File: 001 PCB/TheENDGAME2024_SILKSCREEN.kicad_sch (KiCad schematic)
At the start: 78 parts, among them J1 B+, J2 B-, SW1 SW_SPDT, SW10 SW_Push, SW11 SW_Push, SW12 SW_Push, SW13 SW_Push, SW14 SW_Push, SW15 SW_Push, SW16 SW_Push, SW17 SW_Push, SW18 SW_Push, SW19 SW_Push, SW2 SW_Push, SW20 SW_Push, SW21 SW_Push, SW22 SW_Push, SW23 SW_Push, SW24 SW_Push, SW25 SW_Push, SW26 SW_Push, SW27 SW_Push, SW28 SW_Push, SW29 SW_Push, SW3 SW_Push, SW30 SW_Push, SW31 SW_Push, SW32 SW_Push, SW33 SW_Push, SW34 SW_Push, SW35 SW_Push, SW36 SW_Push, SW37 SW_Push, SW38 SW_Push, SW4 SW_Push, SW5 SW_Push, SW6 SW_Push, SW7 SW_Push, SW8 SW_Push, SW9 SW_Push, U1 SuperMini nRF52840, U2 RP2040-Zero_stolen_from_Purox

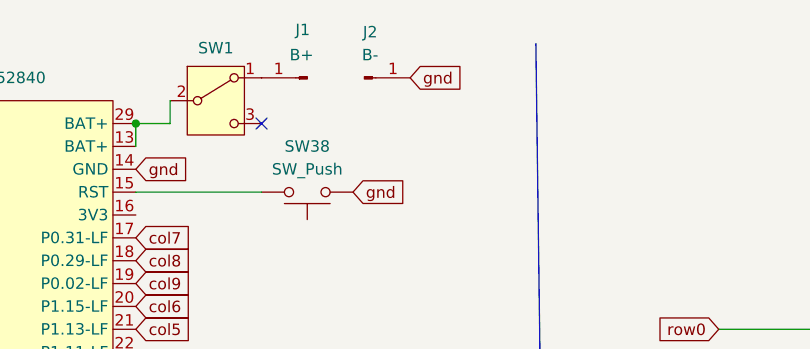
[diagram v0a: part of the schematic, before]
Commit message: added changed Battery connection pads to JST PicoBlade connector
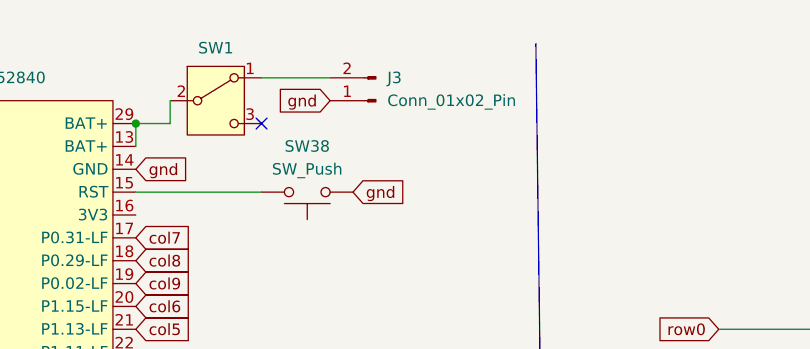
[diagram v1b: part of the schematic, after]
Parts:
- removed J1: B+, Connector_Wire:SolderWirePad_1x01_SMD_1x2mm, symbol Connector:Conn_01x01_Pin
- removed J2: B-, Connector_Wire:SolderWirePad_1x01_SMD_1x2mm, symbol Connector:Conn_01x01_Pin
- added J3: Conn_01x02_Pin, Connector_Molex:Molex_PicoBlade_53048-0210_1x02_P1.25mm_Horizontal, symbol Connector:Conn_01x02_Pin
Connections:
- net gnd: now also J3.1 (Pin_1)
- net at SW1.1 (A): now also J3.2 (Pin_2)
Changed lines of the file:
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@@
 	(wire
 		(pts
+			(xy 82.55 17.78) (xy 74.93 17.78)
+		)
+		(stroke
+			(width 0)
+			(type default)
+		)
+	)
+	(wire
+		(pts
 			(xy 273.05 40.64) (xy 273.05 58.42)
 		)
@@
 	(global_label "gnd"
 		(shape input)
-		(at 91.44 17.78 0)
+		(at 82.55 20.32 180)
 		(fields_autoplaced yes)
 		(effects
@@
 				(size 1.27 1.27)
 			)
-			(justify left)
+			(justify right)
 		)
 		(property "Intersheetrefs" "${INTERSHEET_REFS}"
-			(at 97.8722 17.78 0)
+			(at 76.1178 20.32 0)
 			(effects
 				(font
 					(size 1.27 1.27)
 				)
-				(justify left)
+				(justify right)
 				(hide yes)
 			)
@@
 	)
 	(symbol
-		(lib_id "Connector:Conn_01x01_Pin")
-		(at 80.01 17.78 180)
+		(lib_id "Connector:Conn_01x02_Pin")
+		(at 87.63 20.32 180)
 		(unit 1)
 		(exclude_from_sim no)
@@
 		(on_board yes)
 		(dnp no)
-		(property "Reference" "J1"
-			(at 79.502 12.446 0)
+		(fields_autoplaced yes)
+		(property "Reference" "J3"
+			(at 88.9 17.7799 0)
 			(effects
 				(font
 					(size 1.27 1.27)
 				)
+				(justify right)
 			)
 		)
-		(property "Value" "B+"
-			(at 79.375 15.24 0)
+		(property "Value" "Conn_01x02_Pin"
+			(at 88.9 20.3199 0)
 			(effects
 				(font
 					(size 1.27 1.27)
 				)
+				(justify right)
 			)
 		)
-		(property "Footprint" "Connector_Wire:SolderWirePad_1x01_SMD_1x2mm"
-			(at 80.01 17.78 0)
+		(property "Footprint" "Connector_Molex:Molex_PicoBlade_53048-0210_1x02_P1.25mm_Horizontal"
+			(at 87.63 20.32 0)
 			(effects
 				(font
@@
 		)
 		(property "Datasheet" "~"
-			(at 80.01 17.78 0)
+			(at 87.63 20.32 0)
 			(effects
 				(font
@@
 			)
 		)
-		(property "Description" "Generic connector, single row, 01x01, script generated"
-			(at 80.01 17.78 0)
+		(property "Description" "Generic connector, single row, 01x02, script generated"
+			(at 87.63 20.32 0)
 			(effects
 				(font
@@
 		(pin "1"
 		)
+		(pin "2"
+		)
 		(instances
-			(project "TheENDGAME2024_SILKSCREEN"
+			(project ""
 				(path "/1a30e4b6-03d7-4c78-8024-353d1219867a"
-					(reference "J1")
+					(reference "J3")
 					(unit 1)
 				)
@@
 					(unit 1)
 				)
-			)
-		)
-	)
-	(symbol
-		(lib_id "Connector:Conn_01x01_Pin")
-		(at 86.36 17.78 0)
-		(unit 1)
-		(exclude_from_sim no)
-		(in_bom yes)
-		(on_board yes)
-		(dnp no)
-		(fields_autoplaced yes)
-		(property "Reference" "J2"
-			(at 86.995 12.7 0)
-			(effects
-				(font
-					(size 1.27 1.27)
-				)
-			)
-		)
-		(property "Value" "B-"
-			(at 86.995 15.24 0)
-			(effects
-				(font
-					(size 1.27 1.27)
-				)
-			)
-		)
-		(property "Footprint" "Connector_Wire:SolderWirePad_1x01_SMD_1x2mm"
-			(at 86.36 17.78 0)
-			(effects
-				(font
-					(size 1.27 1.27)
-				)
-				(hide yes)
-			)
-		)
-		(property "Datasheet" "~"
-			(at 86.36 17.78 0)
-			(effects
-				(font
-					(size 1.27 1.27)
-				)
-				(hide yes)
-			)
-		)
-		(property "Description" "Generic connector, single row, 01x01, script generated"
-			(at 86.36 17.78 0)
-			(effects
-				(font
-					(size 1.27 1.27)
-				)
-				(hide yes)
-			)
-		)
-		(pin "1"
-		)
-		(instances
-			(project ""
-				(path "/1a30e4b6-03d7-4c78-8024-353d1219867a"
-					(reference "J2")
-					(unit 1)
-				)
